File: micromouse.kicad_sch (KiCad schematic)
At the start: 12 parts, among them SW1 SW_SPDT_312, SW2 SW_Push, U5 ROB-14450, U6 VL53L0X, U7 VL53L0X, U8 VL53L0X

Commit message: footprints
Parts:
- removed SW1: SW_SPDT_312, symbol Switch:SW_SPDT_312
- removed U2: ~, symbol stm 32 black pill:STM32F411CEU6_
- added SW1: SW_SPST, symbol Switch:SW_SPST
- added U2: STM32 Blackpill, STM32:STM32, symbol STM32 blackpill:STM32F411CEU6_
- U3: value ~ -> N20 encoder right
- U4: value ~ -> N20 encoder left
- U5: value ROB-14450 -> TB6612FNG; footprint ROB-14450:MODULE_ROB-14450 -> TB6612FNG:TB6612FNG
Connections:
- net 3.3v: now also U2. (VB)
- net 5v: now also U2. (VB)
- net 7.4v: now also SW1.1 (A)
- net 7.4vb: now also SW1.2 (B)
- net AIN1: now also U2. (VB)
- net AIN2: now also U2. (VB)
- net BIN1: now also U2. (VB)
- net BIN2: now also U2. (VB)
- net GND: now also U2. (VB)
- net PWM A: now also U2. (VB)
- net PWM B: now also U2. (VB)
- net SCL: now also U2. (VB)
- net SDA: now also U2. (VB)
- net STBY: now also U2. (VB)
- net XSHUT 1: now also U2. (VB)
- net XSHUT 2: now also U2. (VB)
- net XSHUT 3: now also U2. (VB)
- net encoder A1: now also U2. (VB)
- net encoder A2: now also U2. (VB)
- net encoder B1: now also U2. (VB)
- net encoder B2: now also U2. (VB)
- net push button: now also U2. (VB)

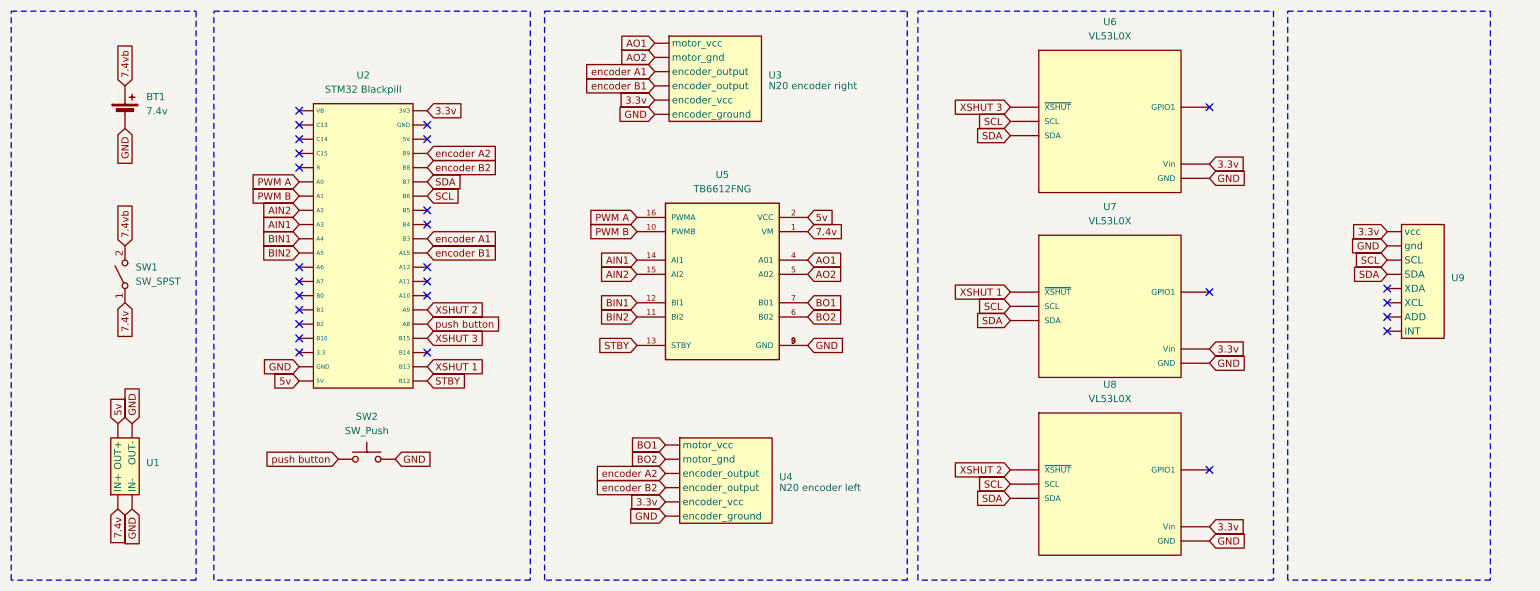
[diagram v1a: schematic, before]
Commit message: footprint changes
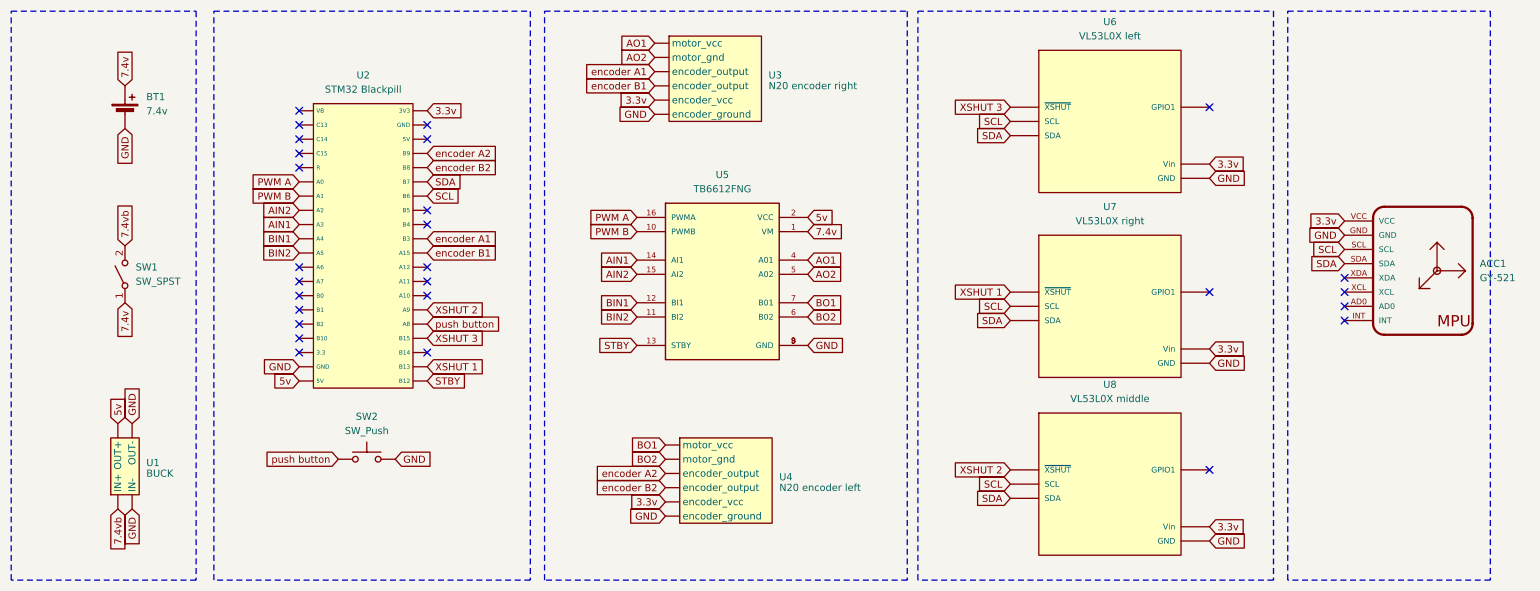
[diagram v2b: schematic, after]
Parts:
- removed U9: ~, symbol mpu 6050:mpu_6050
- added ACC1: GY-521, GY-521:GY-521_SMD, symbol GY521:GY-521
- SW1: footprint (none) -> SPST:JUDCOSPST
- U1: value ~ -> BUCK
- U6: value VL53L0X -> VL53L0X left; footprint VL53L0X:SENSOR_VL53L0X -> VL53L0X:VL53L0X
- U7: value VL53L0X -> VL53L0X right; footprint VL53L0X:SENSOR_VL53L0X -> VL53L0X:VL53L0X
- U8: value VL53L0X -> VL53L0X middle; footprint VL53L0X:SENSOR_VL53L0X -> VL53L0X:VL53L0X
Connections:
- net 3.3v: now also ACC1.VCC
- net 7.4v: now also BT1.1 (+); no longer U1. (OUT-)
- net 7.4vb: now also U1. (OUT-); no longer BT1.1 (+)
- net GND: now also ACC1.GND
- net SCL: now also ACC1.SCL
- net SDA: now also ACC1.SDA
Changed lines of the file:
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@@
 	)
 	(no_connect
-		(at 261.62 89.535)
+		(at 254 87.63)
 	)
 	(no_connect
@@
 	)
 	(no_connect
-		(at 261.62 97.155)
+		(at 254 95.25)
 	)
 	(no_connect
@@
 	)
 	(no_connect
-		(at 261.62 94.615)
+		(at 254 92.71)
 	)
 	(no_connect
@@
 	)
 	(no_connect
-		(at 261.62 92.075)
+		(at 254 90.17)
 	)
 	(rectangle
@@
 	(global_label "GND"
 		(shape input)
-		(at 261.62 81.915 180)
+		(at 254 80.01 180)
 		(fields_autoplaced yes)
 		(effects
@@
 		)
 		(property "Intersheetrefs" "${INTERSHEET_REFS}"
-			(at 254.7643 81.915 0)
+			(at 247.1443 80.01 0)
 			(effects
 				(font
@@
 	(global_label "3.3v"
 		(shape input)
-		(at 261.62 79.375 180)
+		(at 254 77.47 180)
 		(fields_autoplaced yes)
 		(effects
@@
 		)
 		(property "Intersheetrefs" "${INTERSHEET_REFS}"
-			(at 254.6434 79.375 0)
+			(at 247.0234 77.47 0)
 			(effects
 				(font
@@
 		)
 	)
+	(global_label "7.4vb"
+		(shape input)
+		(at 34.925 128.905 270)
+		(fields_autoplaced yes)
+		(effects
+			(font
+				(size 1.27 1.27)
+			)
+			(justify right)
+		)
+		(property "Intersheetrefs" "${INTERSHEET_REFS}"
+			(at 34.925 137.0306 90)
+			(effects
+				(font
+					(size 1.27 1.27)
+				)
+				(justify right)
+				(hide yes)
+			)
+		)
+	)
 	(global_label "SDA"
 		(shape input)
@@
 		)
 	)
-	(global_label "7.4vb"
+	(global_label "7.4v"
 		(shape input)
 		(at 36.195 53.34 90)
@@
 		)
 		(property "Intersheetrefs" "${INTERSHEET_REFS}"
-			(at 36.195 45.2144 90)
+			(at 36.195 46.3634 90)
 			(effects
 				(font
@@
 	(global_label "SDA"
 		(shape input)
-		(at 261.62 86.995 180)
+		(at 254 85.09 180)
 		(fields_autoplaced yes)
 		(effects
@@
 		)
 		(property "Intersheetrefs" "${INTERSHEET_REFS}"
-			(at 255.0667 86.995 0)
+			(at 247.4467 85.09 0)
 			(effects
 				(font
@@
 	(global_label "SCL"
 		(shape input)
-		(at 261.62 84.455 180)
+		(at 254 82.55 180)
 		(fields_autoplaced yes)
 		(effects
@@
 		)
 		(property "Intersheetrefs" "${INTERSHEET_REFS}"
-			(at 255.1272 84.455 0)
+			(at 247.5072 82.55 0)
 			(effects
 				(font
@@
 		)
 	)
-	(global_label "7.4v"
-		(shape input)
-		(at 34.925 128.905 270)
-		(fields_autoplaced yes)
-		(effects
-			(font
-				(size 1.27 1.27)
-			)
-			(justify right)
-		)
-		(property "Intersheetrefs" "${INTERSHEET_REFS}"
-			(at 34.925 135.8816 90)
-			(effects
-				(font
-					(size 1.27 1.27)
-				)
-				(justify right)
-				(hide yes)
-			)
-		)
-	)
 	(global_label "SCL"
 		(shape input)
@@
 	)
 	(symbol
-		(lib_id "mpu 6050:mpu_6050")
-		(at 267.97 86.995 0)
+		(lib_id "GY521:GY-521")
+		(at 270.51 86.36 0)
 		(unit 1)
 		(exclude_from_sim no)
@@
 		(dnp no)
 		(fields_autoplaced yes)
-		(property "Reference" "U9"
-			(at 273.05 87.6299 0)
+		(property "Reference" "ACC1"
+			(at 278.13 85.0899 0)
 			(effects
 				(font
@@
 			)
 		)
-		(property "Value" "~"
-			(at 273.05 89.535 0)
+		(property "Value" "GY-521"
+			(at 278.13 87.6299 0)
 			(effects
 				(font
@@
 			)
 		)
-		(property "Footprint" ""
-			(at 267.97 86.995 0)
+		(property "Footprint" "GY-521:GY-521_SMD"
+			(at 270.51 86.36 0)
 			(effects
 				(font
@@
 		)
 		(property "Datasheet" ""
-			(at 267.97 86.995 0)
+			(at 270.51 86.36 0)
 			(effects
 				(font
@@
 		)
 		(property "Description" ""
-			(at 267.97 86.995 0)
+			(at 270.51 86.36 0)
 			(effects
 				(font
@@
 			)
 		)
-		(pin ""
+		(property "MF" "GODREAM FORDREAM CO., LIMITED"
+			(at 270.51 86.36 0)
+			(effects
+				(font
+					(size 1.27 1.27)
+				)
+				(justify bottom)
+				(hide yes)
+			)
 		)
-		(pin ""
+		(property "Description_1" "\n                        \n                            Triple Axis Accelerometer Gyro Breakout\n                        \n"
+			(at 270.51 86.36 0)
+			(effects
+				(font
+					(size 1.27 1.27)
+				)
+				(justify bottom)
+				(hide yes)
+			)
 		)
-		(pin ""
+		(property "Package" "Package"
+			(at 270.51 86.36 0)
+			(effects
+				(font
+					(size 1.27 1.27)
+				)
+				(justify bottom)
+				(hide yes)
+			)
 		)
-		(pin ""
+		(property "Price" "None"
+			(at 270.51 86.36 0)
+			(effects
+				(font
+					(size 1.27 1.27)
+				)
+				(justify bottom)
+				(hide yes)
+			)
 		)
-		(pin ""
+		(property "SnapEDA_Link" "https://www.snapeda.com/parts/GY-521/GODREAM+FORDREAM+CO.%252C+LIMITED/view-part/?ref=snap"
+			(at 270.51 86.36 0)
+			(effects
+				(font
+					(size 1.27 1.27)
+				)
+				(justify bottom)
+				(hide yes)
+			)
 		)
-		(pin ""
+		(property "MP" "GY-521"
+			(at 270.51 86.36 0)
+			(effects
+				(font
+					(size 1.27 1.27)
+				)
+				(justify bottom)
+				(hide yes)
+			)
 		)
-		(pin ""
+		(property "Availability" "Not in stock"
+			(at 270.51 86.36 0)
+			(effects
+				(font
+					(size 1.27 1.27)
+				)
+				(justify bottom)
+				(hide yes)
+			)
 		)
-		(pin ""
+		(property "Check_prices" "https://www.snapeda.com/parts/GY-521/GODREAM+FORDREAM+CO.%252C+LIMITED/view-part/?ref=eda"
+			(at 270.51 86.36 0)
+			(effects
+				(font
+					(size 1.27 1.27)
+				)
+				(justify bottom)
+				(hide yes)
+			)
+		)
+		(pin "AD0"
+		)
+		(pin "GND"
+		)
+		(pin "SCL"
+		)
+		(pin "SDA"
+		)
+		(pin "VCC"
+		)
+		(pin "XCL"
+		)
+		(pin "XDA"
+		)
+		(pin "INT"
 		)
 		(instances
 			(project ""
 				(path "/ad2eaac4-906f-408a-b5e5-135c4e396716"
-					(reference "U9")
+					(reference "ACC1")
 					(unit 1)
 				)
@@
 			)
 		)
-		(property "Value" "VL53L0X"
+		(property "Value" "VL53L0X middle"
 			(at 212.09 109.22 0)
 			(effects
@@
 			)
 		)
-		(property "Footprint" "VL53L0X:SENSOR_VL53L0X"
+		(property "Footprint" "VL53L0X:VL53L0X"
 			(at 253.238 153.67 0)
 			(effects
@@
 	)
 	(symbol
-		(lib_name "encoder motor:encoder_motor")
 		(lib_id "encoder motor:encoder_motor")
 		(at 140.335 121.285 0)
@@
 			)
 		)
-		(property "Value" "~"
+		(property "Value" "BUCK"
 			(at 40.005 122.555 90)
 			(effects
@@
 			)
 		)
-		(property "Value" "VL53L0X"
+		(property "Value" "VL53L0X right"
 			(at 212.09 77.47 0)
 			(effects
@@
 			)
 		)
-		(property "Footprint" "VL53L0X:SENSOR_VL53L0X"
+		(property "Footprint" "VL53L0X:VL53L0X"
 			(at 253.238 121.92 0)
 			(effects
@@
 			)
 		)
-		(property "Value" "VL53L0X"
+		(property "Value" "VL53L0X left"
 			(at 212.09 44.45 0)
 			(effects
@@
 			)
 		)
-		(property "Footprint" "VL53L0X:SENSOR_VL53L0X"
+		(property "Footprint" "VL53L0X:VL53L0X"
 			(at 253.238 88.9 0)
 			(effects
@@
 			)
 		)
-		(property "Footprint" ""
+		(property "Footprint" "SPST:JUDCOSPST"
 			(at 36.195 86.995 0)
 			(effects

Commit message: push button and buck footprint
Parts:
- U5: footprint TB6612FNG:TB6612FNG -> Tb6612fng:TB6612FNG
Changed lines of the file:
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@@
 	)
 	(symbol
-		(lib_name "VL53L0X:VL53L0X")
 		(lib_id "VL53L0X:VL53L0X")
 		(at 208.28 147.32 0)
@@
 			)
 		)
-		(property "Footprint" "TB6612FNG:TB6612FNG"
+		(property "Footprint" "Tb6612fng:TB6612FNG"
 			(at 142.875 89.535 0)
 			(effects
@@
 	)
 	(symbol
-		(lib_name "VL53L0X:VL53L0X")
 		(lib_id "VL53L0X:VL53L0X")
 		(at 208.28 115.57 0)
@@
 	)
 	(symbol
-		(lib_name "VL53L0X:VL53L0X")
 		(lib_id "VL53L0X:VL53L0X")
 		(at 208.28 82.55 0)

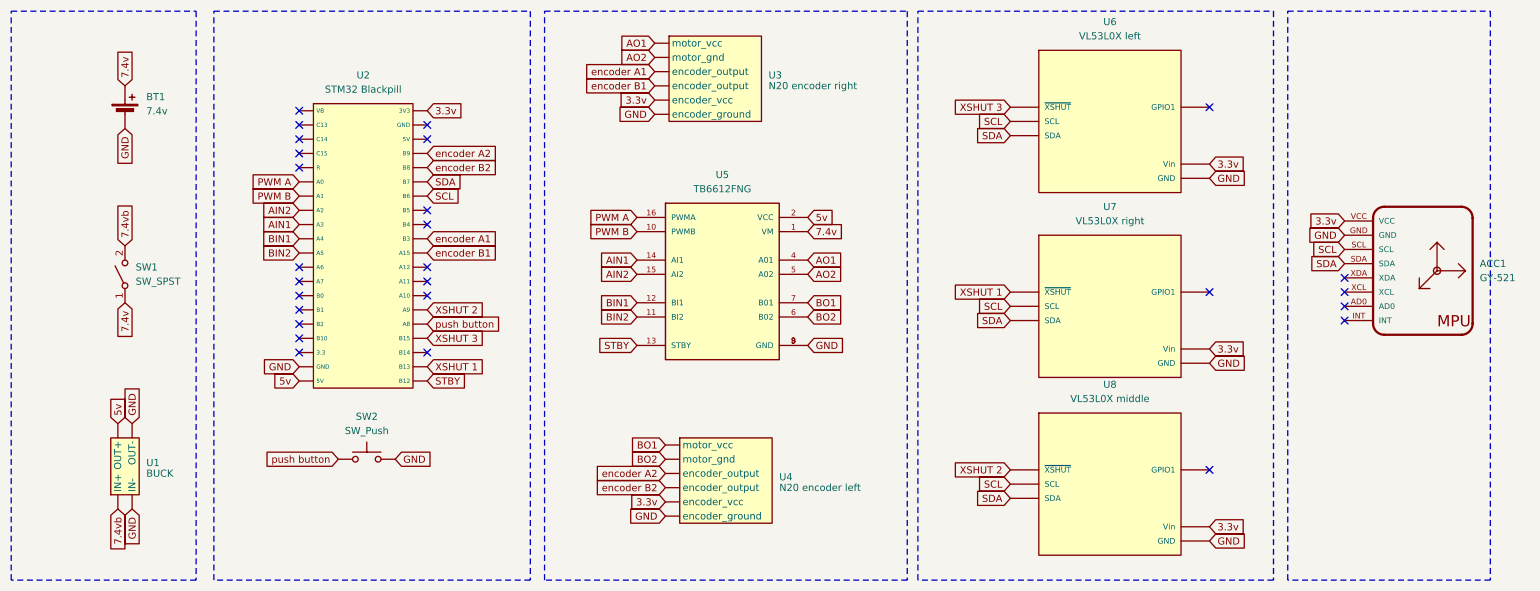
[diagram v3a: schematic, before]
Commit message: schematic changes, and footprint assignment
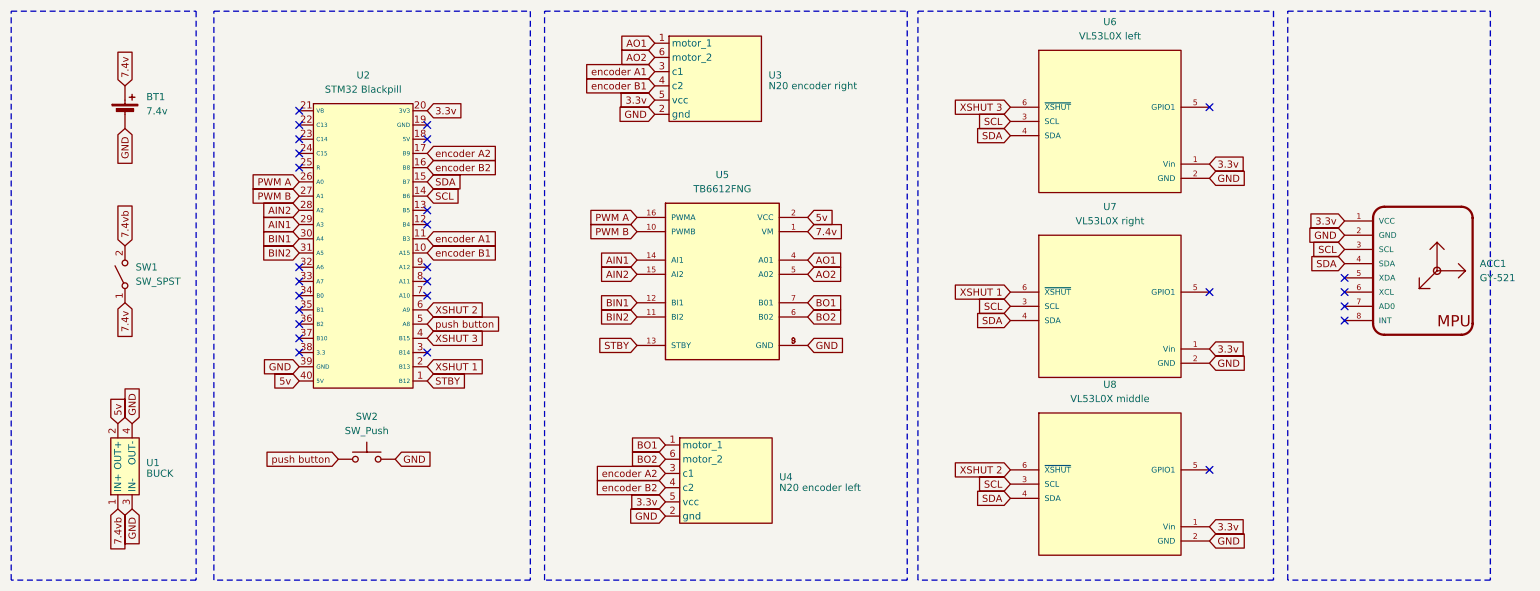
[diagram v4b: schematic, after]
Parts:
- SW2: footprint (none) -> push button:push_button
- U1: footprint (none) -> buck:buck
- U3, U4: footprint (none) -> Connector_PinHeader_2.00mm:PinHeader_1x06_P2.00mm_Vertical
- U5: footprint Tb6612fng:TB6612FNG -> TB6612FNG:TB6612FNG; Availability In Stock -> (none); Description_1 TB6612FNG - Motor Controller/Driver Power Management Evalua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 -> (none); MANUFACTURER Sparkfun Electronics -> (none); MF SparkFun Electronics -> (none); PARTREV 11-13-17 -> (none); Package None -> (none); Price None -> (none); STANDARD Manufacturer Recommendation -> (none); SnapEDA_Link https://www.snapeda.com/parts/ROB-14450/SparkFun/view-part/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 -> (none)
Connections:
- net 3.3v: now also ACC1.1 (VCC), U2.20 (3V3), U3.5 (vcc), U4.5 (vcc), U6.1 (Vin), U7.1 (Vin), U8.1 (Vin); no longer ACC1.VCC, U2. (VB), U3. (motor_vcc), U4. (motor_vcc), U6. (~{XSHUT}), U7. (~{XSHUT}), U8. (~{XSHUT})
- net 5v: now also U1.2 (OUT+), U2.40 (5V); no longer U1. (OUT-), U2. (VB)
- net 7.4vb: now also U1.1 (IN+); no longer U1. (OUT-)
- net AIN1: now also U2.29 (A3); no longer U2. (VB)
- net AIN2: now also U2.28 (A2); no longer U2. (VB)
- net AO1: now also U3.1 (motor_1); no longer U3. (motor_vcc)
- net AO2: now also U3.6 (motor_2); no longer U3. (motor_vcc)
- net BIN1: now also U2.30 (A4); no longer U2. (VB)
- net BIN2: now also U2.31 (A5); no longer U2. (VB)
- net BO1: now also U4.1 (motor_1); no longer U4. (motor_vcc)
- net BO2: now also U4.6 (motor_2); no longer U4. (motor_vcc)
- net GND: now also ACC1.2 (GND), U1.3 (IN-), U1.4 (OUT-), U2.39 (GND), U3.2 (gnd), U4.2 (gnd), U6.2 (GND), U7.2 (GND), U8.2 (GND); no longer ACC1.GND, U1. (OUT-), U2. (VB), U3. (motor_vcc), U4. (motor_vcc), U6. (~{XSHUT}), U7. (~{XSHUT}), U8. (~{XSHUT})
- net PWM A: now also U2.26 (A0); no longer U2. (VB)
- net PWM B: now also U2.27 (A1); no longer U2. (VB)
- net SCL: now also ACC1.3 (SCL), U2.14 (B6), U6.3 (SCL), U7.3 (SCL), U8.3 (SCL); no longer ACC1.SCL, U2. (VB), U6. (~{XSHUT}), U7. (~{XSHUT}), U8. (~{XSHUT})
- net SDA: now also ACC1.4 (SDA), U2.15 (B7), U6.4 (SDA), U7.4 (SDA), U8.4 (SDA); no longer ACC1.SDA, U2. (VB), U6. (~{XSHUT}), U7. (~{XSHUT}), U8. (~{XSHUT})
- net STBY: now also U2.1 (B12); no longer U2. (VB)
- net XSHUT 1: now also U2.2 (B13), U7.6 (~{XSHUT}); no longer U2. (VB), U7. (~{XSHUT})
- net XSHUT 2: now also U2.6 (A9), U8.6 (~{XSHUT}); no longer U2. (VB), U8. (~{XSHUT})
- net XSHUT 3: now also U2.4 (B15), U6.6 (~{XSHUT}); no longer U2. (VB), U6. (~{XSHUT})
- net encoder A1: now also U2.11 (B3), U3.3 (c1); no longer U2. (VB), U3. (motor_vcc)
- net encoder A2: now also U2.17 (B9), U4.3 (c1); no longer U2. (VB), U4. (motor_vcc)
- net encoder B1: now also U2.10 (A15), U3.4 (c2); no longer U2. (VB), U3. (motor_vcc)
- net encoder B2: now also U2.16 (B8), U4.4 (c2); no longer U2. (VB), U4. (motor_vcc)
- net push button: now also U2.5 (A8); no longer U2. (VB)

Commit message: schematic and footprint changes
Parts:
- removed BT1: 7.4v, symbol Device:Battery_Cell
- removed U5: TB6612FNG, TB6612FNG:TB6612FNG, symbol tb6612fng:ROB-14450
- added J1: XT60-M, XT60:AMASS_XT60-M, symbol XT60-M:XT60-M
- added U5: TB6612FNG, TB6612FNG:TB6612FNG, symbol TB66:TB6612FNG
- U3, U4: footprint Connector_PinHeader_2.00mm:PinHeader_1x06_P2.00mm_Vertical -> Connector_PinHeader_2.54mm:PinHeader_1x06_P2.54mm_Vertical
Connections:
- net 5v: now also U5.2 (VCC)
- net 7.4v: now also SW1.T (A), J1.P (POS), U5.1 (VM); no longer SW1.1 (A)
- net 7.4vb: now also SW1.P (B); no longer SW1.2 (B)
- net AIN1: now also U5.14 (AI1)
- net AIN2: now also U5.15 (AI2)
- net AO1 : now also U5.4 (A01)
- net AO2: now also U5.5 (A02)
- net BIN1: now also U5.12 (BI1)
- net BIN2: now also U5.11 (BI2)
- net BO1: now also U5.7 (B01)
- net BO2: now also U5.6 (B02)
- net GND: now also J1.N (NEG), U5.3 (GND), U5.8 (GND), U5.9 (GND)
- net PWM A: now also U5.16 (PWMA)
- net PWM B: now also U5.10 (PWMB)
- net STBY: now also U5.13 (STBY)
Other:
- moved on the sheet: SW1, U1

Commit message: routing
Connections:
- net AO1  is gone; now on net AO1: U5.4 (A01)
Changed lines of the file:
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@@
 		)
 	)
-	(global_label "AO1 "
+	(global_label "AO1"
 		(shape input)
 		(at 158.115 84.455 0)
@@
 		)
 		(property "Intersheetrefs" "${INTERSHEET_REFS}"
-			(at 165.6964 84.455 0)
+			(at 164.7288 84.455 0)
 			(effects
 				(font

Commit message: ll
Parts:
- added SW3: SW_Push, push button:push_button, symbol Switch:SW_Push
- U5: footprint TB6612FNG:TB6612FNG -> Tb6612fng:TB6612FNG
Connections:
- net GND: now also SW3.2
- net push button 1: now reaches U2.13 (B5)
- net push button 1: now also SW3.1
- no-connect marks 27 -> 26
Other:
- moved on the sheet: U2

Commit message: pcb changes
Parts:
- added SW4: SW_SPDT_312, slide switch:SLIDE SW, symbol Switch:SW_SPDT_312
- U5: footprint Tb6612fng:TB6612FNG -> TB6612FNG:TB6612FNG
- renumbered SW3 to SW2, SW2 to SW3
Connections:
- net 3.3v: now also SW4.2 (C)
- net GND: now also SW4.3 (A)
- new net slide_SW: SW4.1 (B)
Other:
- moved on the sheet: SW2, SW3, U2
